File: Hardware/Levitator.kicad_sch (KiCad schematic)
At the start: 11 parts, among them Q1 BUK7880-55A, Q2 NMOS, U1 LM358, U2 A1301EUA-T

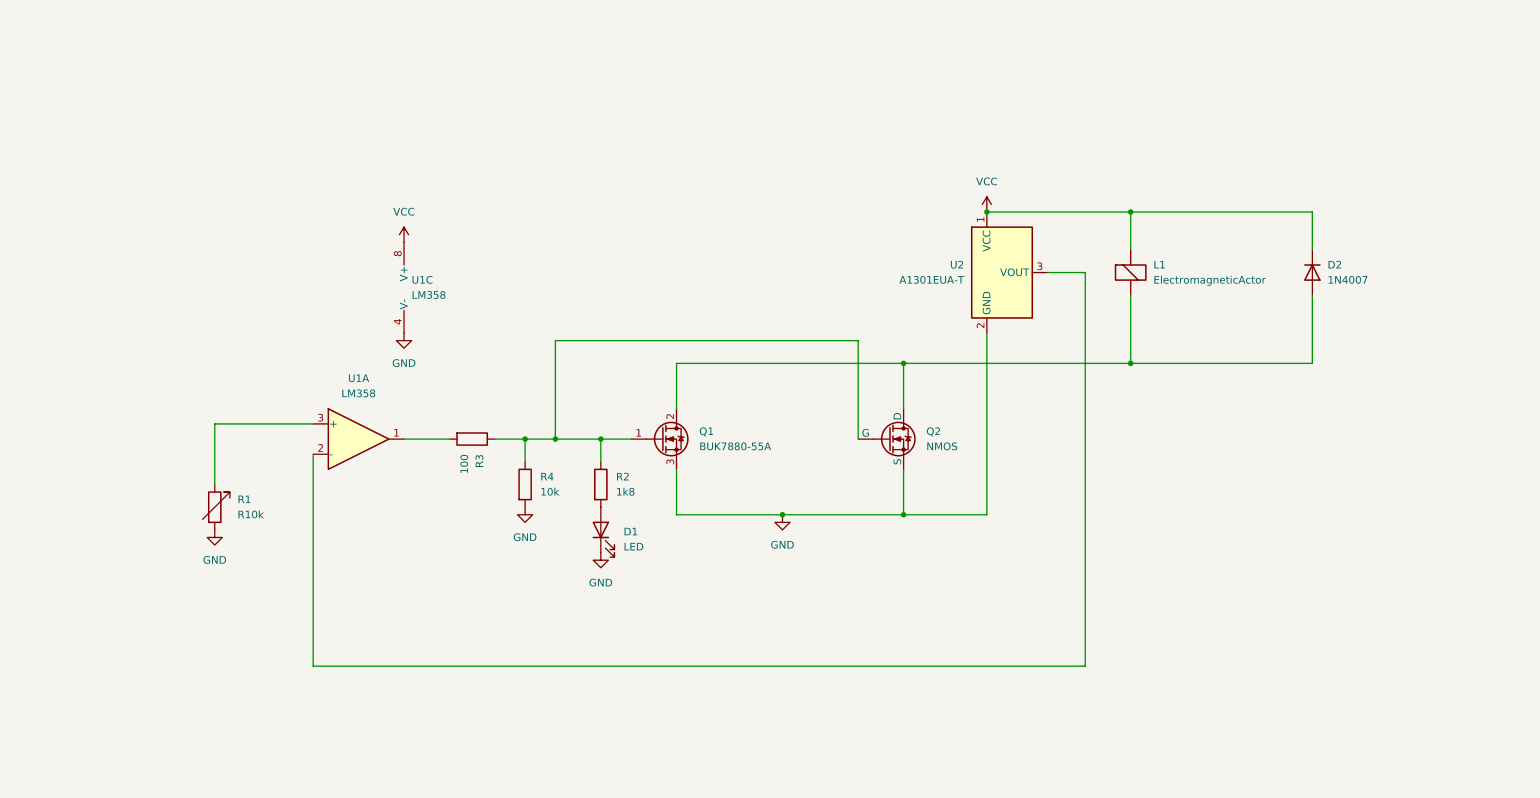
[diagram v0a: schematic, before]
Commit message: feat: Modified to use dual supplies, and tidied up
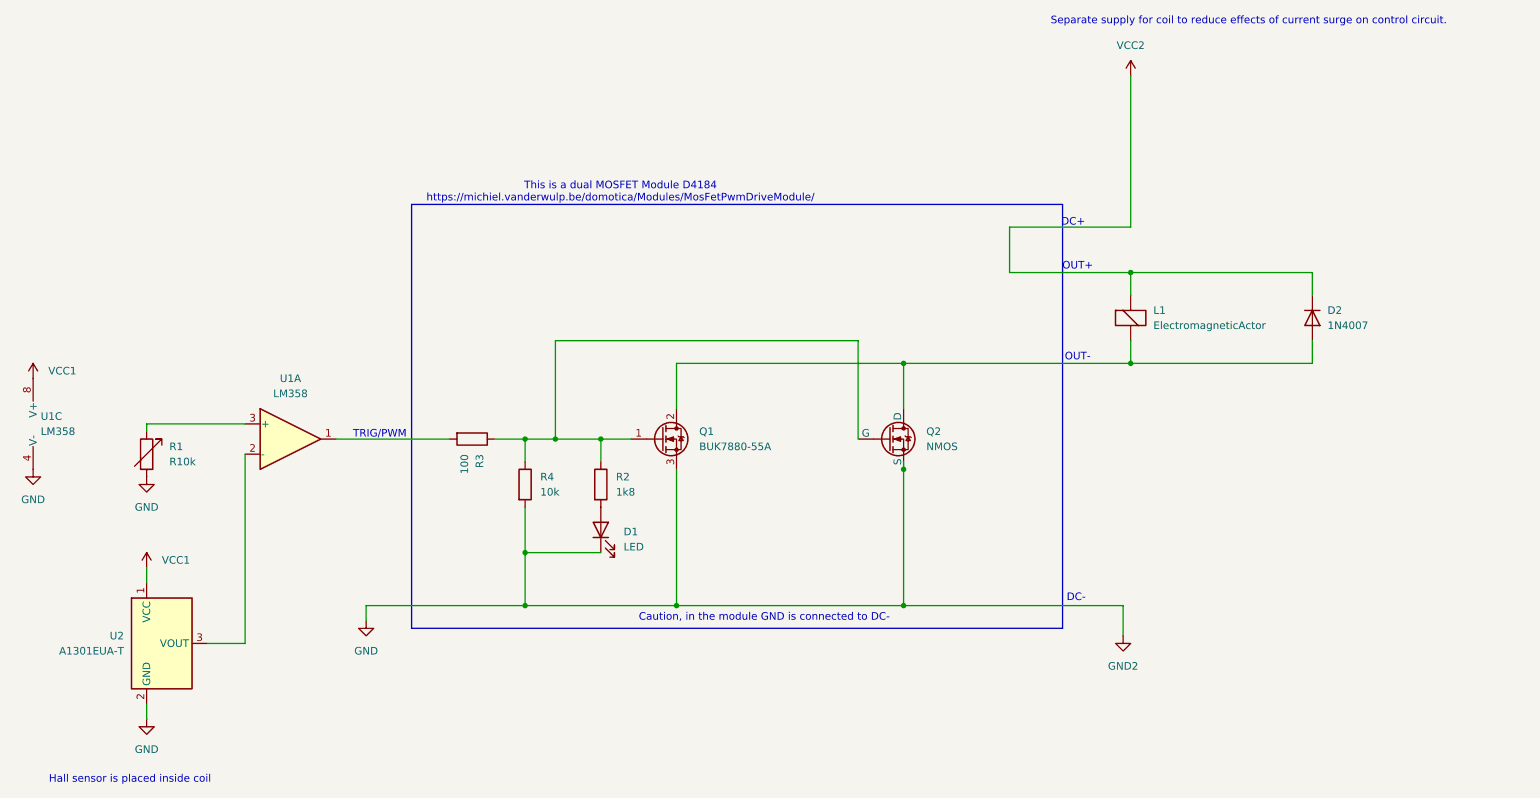
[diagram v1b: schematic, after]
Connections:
- net VCC renamed VCC1
- net VCC1: no longer D2.1 (K), L1.1 (-)
- new net VCC2: D2.1 (K), L1.1 (-)
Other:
- note added: "Caution, in the module GND is connected to DC-"
- note added: "DC+"
- note added: "DC-"
- note added: "Hall sensor is placed inside coil"
- note added: "OUT+"
- note added: "OUT-"
- note added: "Separate supply for coil to reduce effects of current surge on control circuit."
- note added: "TRIG/PWM"
- note added: "This is a dual MOSFET Module D4184 https://michiel.vanderwulp.be/domotica/Modules/MosFetPwmDriveModule/"
- company: (none) -> Neil Pate
- title: (none) -> Levitator
- moved on the sheet: D2, L1, R1, U1A, U1C, U2

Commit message: feat: Updated schematic to use single MOSFET and added PCB layout
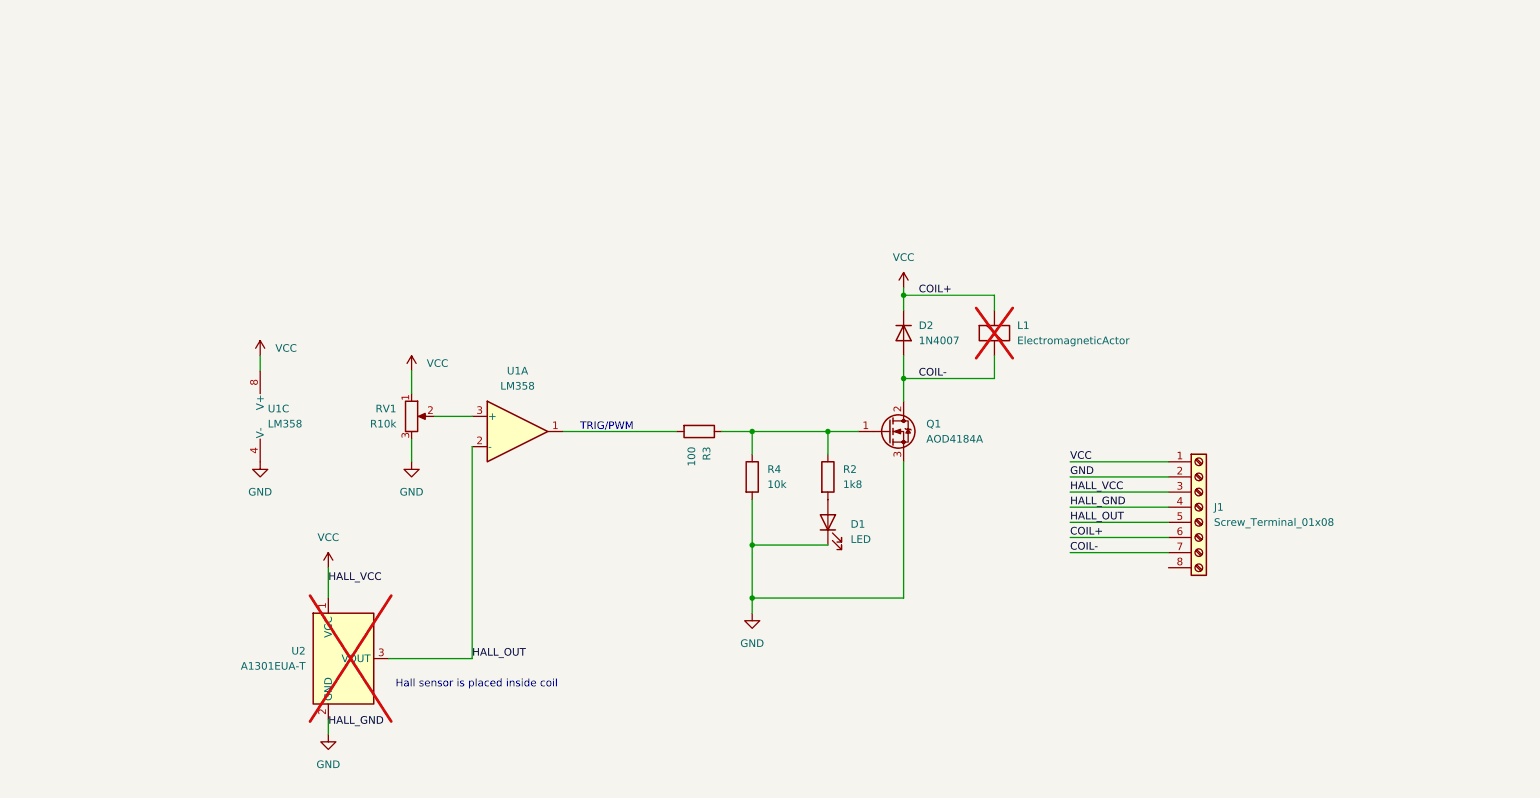
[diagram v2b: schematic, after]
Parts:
- removed Q2: NMOS, symbol Simulation_SPICE:NMOS
- removed R1: R10k, symbol Device:R_Variable
- added J1: Screw_Terminal_01x08, TerminalBlock:TerminalBlock_bornier-8_P5.08mm, symbol Connector:Screw_Terminal_01x08
- added RV1: R10k, TerminalBlock:TerminalBlock_bornier-3_P5.08mm, symbol Device:R_Potentiometer
- D1: footprint (none) -> LED_THT:LED_D3.0mm
- L1, U2: now not fitted
- Q1: value BUK7880-55A -> AOD4184A; footprint Package_TO_SOT_SMD:SOT-223-3_TabPin2 -> Package_TO_SOT_THT:TO-220-3_Vertical
- R2, R3, R4: footprint (none) -> Resistor_THT:R_Axial_DIN0204_L3.6mm_D1.6mm_P5.08mm_Horizontal
- U1: footprint (none) -> Package_DIP:DIP-8_W7.62mm_Socket
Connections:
- net VCC2 is gone; now on net VCC: D2.1 (K), L1.1 (-)
- net GND: now also J1.2 (Pin_2), J1.4 (Pin_4), RV1.3
- net COIL-: now reaches D2.2 (A), L1.2 (+), Q1.2 (D)
- net COIL-: now also J1.7 (Pin_7)
- net HALL_OUT: now reaches U1.2 (-), U2.3 (VOUT)
- net HALL_OUT: now also J1.5 (Pin_5)
- net at U1.3 (+): now also RV1.2
- net VCC1 renamed VCC
- net VCC: now also J1.1 (Pin_1), J1.3 (Pin_3), J1.6 (Pin_6), RV1.1
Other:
- note removed: "Caution, in the module GND is connected to DC-"
- note removed: "DC+"
- note removed: "DC-"
- note removed: "OUT+"
- note removed: "OUT-"
- note removed: "Separate supply for coil to reduce effects of current surge on control circuit."
- note removed: "This is a dual MOSFET Module D4184 https://michiel.vanderwulp.be/domotica/Modules/MosFetPwmDriveModule/"
- moved on the sheet: D1, D2, Q1, R2, R3, R4, U1A, U1C

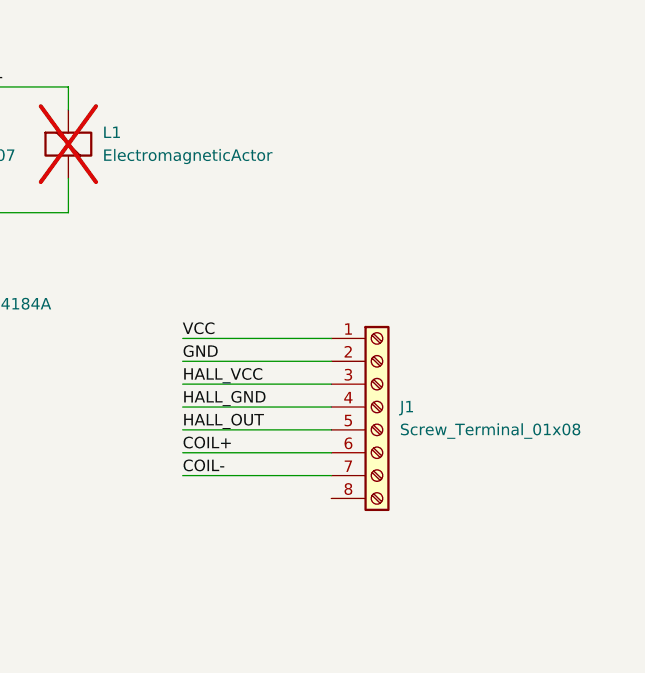
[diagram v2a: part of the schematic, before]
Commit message: feat: Moved power in to barrel socket
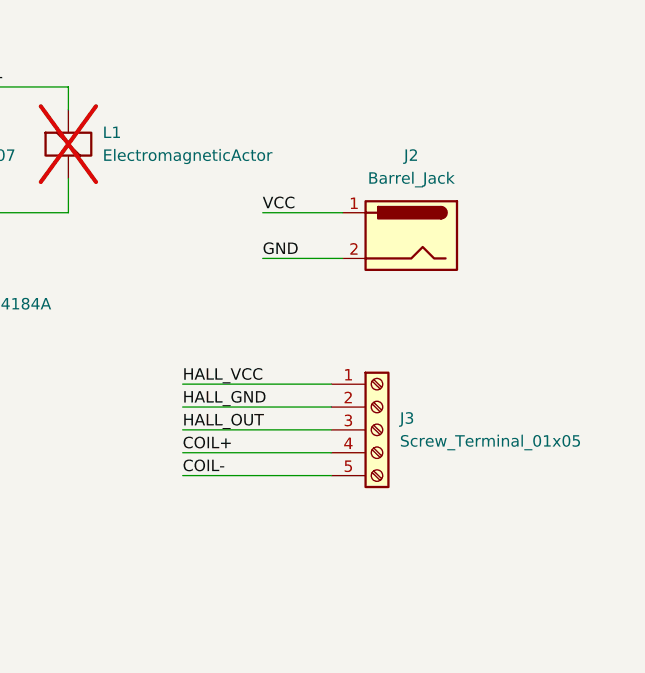
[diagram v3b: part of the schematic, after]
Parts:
- removed J1: Screw_Terminal_01x08, TerminalBlock:TerminalBlock_bornier-8_P5.08mm, symbol Connector:Screw_Terminal_01x08
- added J2: Barrel_Jack, Connector_BarrelJack:BarrelJack_Horizontal, symbol Connector:Barrel_Jack
- added J3: Screw_Terminal_01x05, TerminalBlock:TerminalBlock_bornier-5_P5.08mm, symbol Connector:Screw_Terminal_01x05
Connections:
- net COIL-: now also J3.5 (Pin_5)
- net GND: now also J2.2, J3.2 (Pin_2)
- net HALL_OUT: now also J3.3 (Pin_3)
- net VCC: now also J2.1, J3.1 (Pin_1), J3.4 (Pin_4)
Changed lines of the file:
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@@
 	(wire
 		(pts
-			(xy 200.66 95.25) (xy 217.17 95.25)
+			(xy 172.72 63.5) (xy 172.72 64.77)
 		)
 		(stroke
@@
 	(wire
 		(pts
-			(xy 172.72 63.5) (xy 172.72 64.77)
+			(xy 147.32 87.63) (xy 147.32 91.44)
 		)
 		(stroke
@@
 	(wire
 		(pts
-			(xy 147.32 87.63) (xy 147.32 91.44)
+			(xy 64.77 74.93) (xy 64.77 77.47)
 		)
 		(stroke
@@
 	(wire
 		(pts
-			(xy 64.77 74.93) (xy 64.77 77.47)
+			(xy 100.33 125.73) (xy 86.36 125.73)
 		)
 		(stroke
@@
 	(wire
 		(pts
-			(xy 100.33 125.73) (xy 86.36 125.73)
+			(xy 100.33 90.17) (xy 100.33 125.73)
 		)
 		(stroke
@@
 	(wire
 		(pts
-			(xy 100.33 90.17) (xy 100.33 125.73)
+			(xy 209.55 78.74) (xy 218.44 78.74)
 		)
 		(stroke
@@
 	(wire
 		(pts
-			(xy 200.66 102.87) (xy 217.17 102.87)
+			(xy 209.55 83.82) (xy 218.44 83.82)
 		)
 		(stroke
@@
 	(wire
 		(pts
-			(xy 200.66 92.71) (xy 217.17 92.71)
+			(xy 200.66 102.87) (xy 217.17 102.87)
 		)
 		(stroke
@@
 	)
 	(label "GND"
-		(at 200.66 95.25 0)
+		(at 209.55 83.82 0)
 		(fields_autoplaced yes)
 		(effects
@@
 	)
 	(label "VCC"
-		(at 200.66 92.71 0)
+		(at 209.55 78.74 0)
 		(fields_autoplaced yes)
 		(effects
@@
 	)
 	(symbol
+		(lib_id "Connector:Barrel_Jack")
+		(at 226.06 81.28 0)
+		(mirror y)
+		(unit 1)
+		(exclude_from_sim no)
+		(in_bom yes)
+		(on_board yes)
+		(dnp no)
+		(property "Reference" "J2"
+			(at 226.06 72.39 0)
+			(effects
+				(font
+					(size 1.27 1.27)
+				)
+			)
+		)
+		(property "Value" "Barrel_Jack"
+			(at 226.06 74.93 0)
+			(effects
+				(font
+					(size 1.27 1.27)
+				)
+			)
+		)
+		(property "Footprint" "Connector_BarrelJack:BarrelJack_Horizontal"
+			(at 224.79 82.296 0)
+			(effects
+				(font
+					(size 1.27 1.27)
+				)
+				(hide yes)
+			)
+		)
+		(property "Datasheet" "~"
+			(at 224.79 82.296 0)
+			(effects
+				(font
+					(size 1.27 1.27)
+				)
+				(hide yes)
+			)
+		)
+		(property "Description" "DC Barrel Jack"
+			(at 226.06 81.28 0)
+			(effects
+				(font
+					(size 1.27 1.27)
+				)
+				(hide yes)
+			)
+		)
+		(pin "2"
+		)
+		(pin "1"
+		)
+		(instances
+			(project "Levitator"
+				(path "/0870b899-f9e3-44ec-8b87-0295ae22e9f9"
+					(reference "J2")
+					(unit 1)
+				)
+			)
+		)
+	)
+	(symbol
 		(lib_id "Diode:1N4007")
 		(at 172.72 71.12 270)
@@
 	)
 	(symbol
+		(lib_id "Connector:Screw_Terminal_01x05")
+		(at 222.25 102.87 0)
+		(unit 1)
+		(exclude_from_sim no)
+		(in_bom yes)
+		(on_board yes)
+		(dnp no)
+		(fields_autoplaced yes)
+		(property "Reference" "J3"
+			(at 224.79 101.5999 0)
+			(effects
+				(font
+					(size 1.27 1.27)
+				)
+				(justify left)
+			)
+		)
+		(property "Value" "Screw_Terminal_01x05"
+			(at 224.79 104.1399 0)
+			(effects
+				(font
+					(size 1.27 1.27)
+				)
+				(justify left)
+			)
+		)
+		(property "Footprint" "TerminalBlock:TerminalBlock_bornier-5_P5.08mm"
+			(at 222.25 102.87 0)
+			(effects
+				(font
+					(size 1.27 1.27)
+				)
+				(hide yes)
+			)
+		)
+		(property "Datasheet" "~"
+			(at 222.25 102.87 0)
+			(effects
+				(font
+					(size 1.27 1.27)
+				)
+				(hide yes)
+			)
+		)
+		(property "Description" "Generic screw terminal, single row, 01x05, script generated (kicad-library-utils/schlib/autogen/connector/)"
+			(at 222.25 102.87 0)
+			(effects
+				(font
+					(size 1.27 1.27)
+				)
+				(hide yes)
+			)
+		)
+		(pin "4"
+		)
+		(pin "5"
+		)
+		(pin "2"
+		)
+		(pin "1"
+		)
+		(pin "3"
+		)
+		(instances
+			(project "Levitator"
+				(path "/0870b899-f9e3-44ec-8b87-0295ae22e9f9"
+					(reference "J3")
+					(unit 1)
+				)
+			)
+		)
+	)
+	(symbol
 		(lib_id "Device:R")
 		(at 147.32 95.25 0)
@@
 					(unit 1)
 				)
-			)
-		)
-	)
-	(symbol
-		(lib_id "Connector:Screw_Terminal_01x08")
-		(at 222.25 100.33 0)
-		(unit 1)
-		(exclude_from_sim no)
-		(in_bom yes)
-		(on_board yes)
-		(dnp no)
-		(fields_autoplaced yes)
-		(property "Reference" "J1"
-			(at 224.79 100.3299 0)
-			(effects
-				(font
-					(size 1.27 1.27)
-				)
-				(justify left)
-			)
-		)
-		(property "Value" "Screw_Terminal_01x08"
-			(at 224.79 102.8699 0)
-			(effects
-				(font
-					(size 1.27 1.27)
-				)
-				(justify left)
-			)
-		)
-		(property "Footprint" "TerminalBlock:TerminalBlock_bornier-8_P5.08mm"
-			(at 222.25 100.33 0)
-			(effects
-				(font
-					(size 1.27 1.27)
-				)
-				(hide yes)
-			)
-		)
-		(property "Datasheet" "~"
-			(at 222.25 100.33 0)
-			(effects
-				(font
-					(size 1.27 1.27)
-				)
-				(hide yes)
-			)
-		)
-		(property "Description" "Generic screw terminal, single row, 01x08, script generated (kicad-library-utils/schlib/autogen/connector/)"
-			(at 222.25 100.33 0)
-			(effects
-				(font
-					(size 1.27 1.27)
-				)
-				(hide yes)
-			)
-		)
-		(pin "1"
-		)
-		(pin "4"
-		)
-		(pin "7"
-		)
-		(pin "6"
-		)
-		(pin "5"
-		)
-		(pin "8"
-		)
-		(pin "3"
-		)
-		(pin "2"
-		)
-		(instances
-			(project "Levitator"
-				(path "/0870b899-f9e3-44ec-8b87-0295ae22e9f9"
-					(reference "J1")
-					(unit 1)
-				)
